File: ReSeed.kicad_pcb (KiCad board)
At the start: 2 copper layers, 60.8 x 99.9 mm, 52 parts, among them CN1 EDGE_CONNECTOR, CN2 AUDIO_OUT, CN3 AUDIO_IN, CN4 DB9_MALE, Q1 BC549C, SW1 SW_DIGIFIX, U1 MOS_8580, U105 STEPUP_MT3608, U2 CD74HCT4520E, U3 74HCT245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

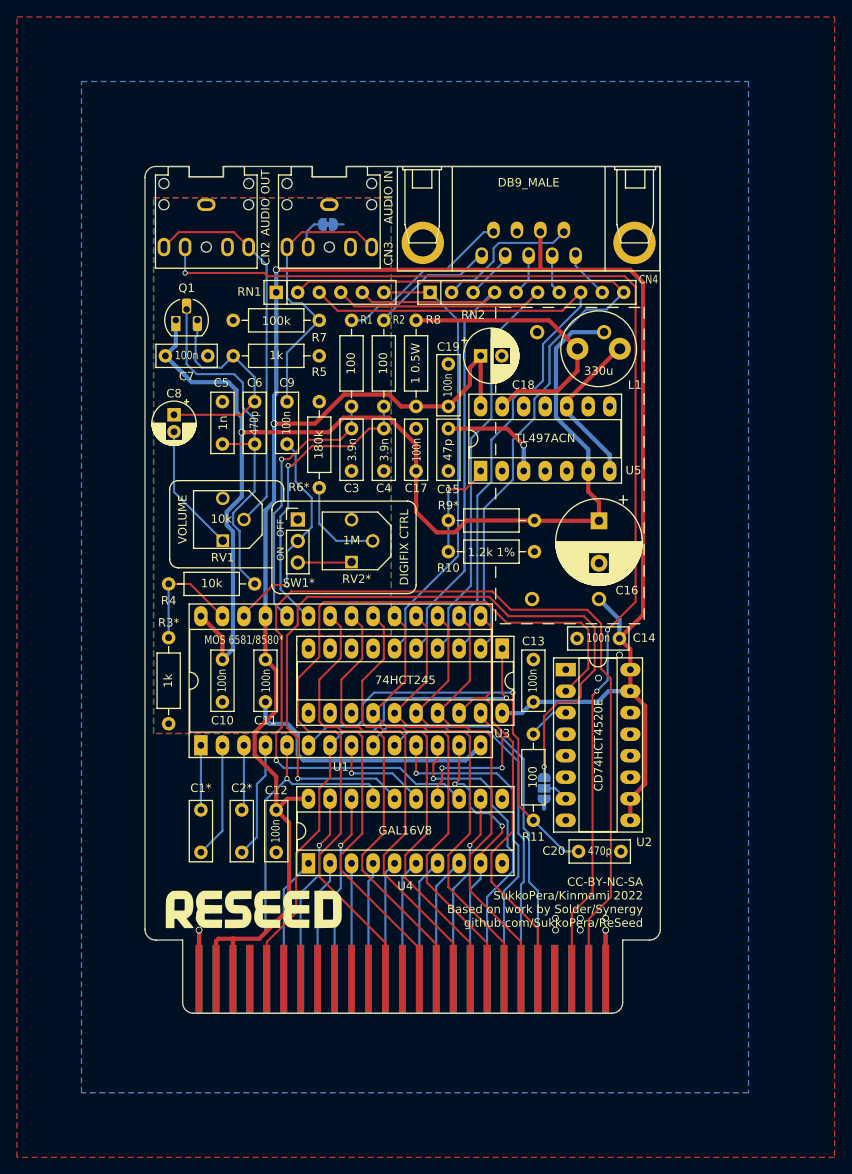
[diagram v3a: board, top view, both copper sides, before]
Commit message: Add ferrites on power lines
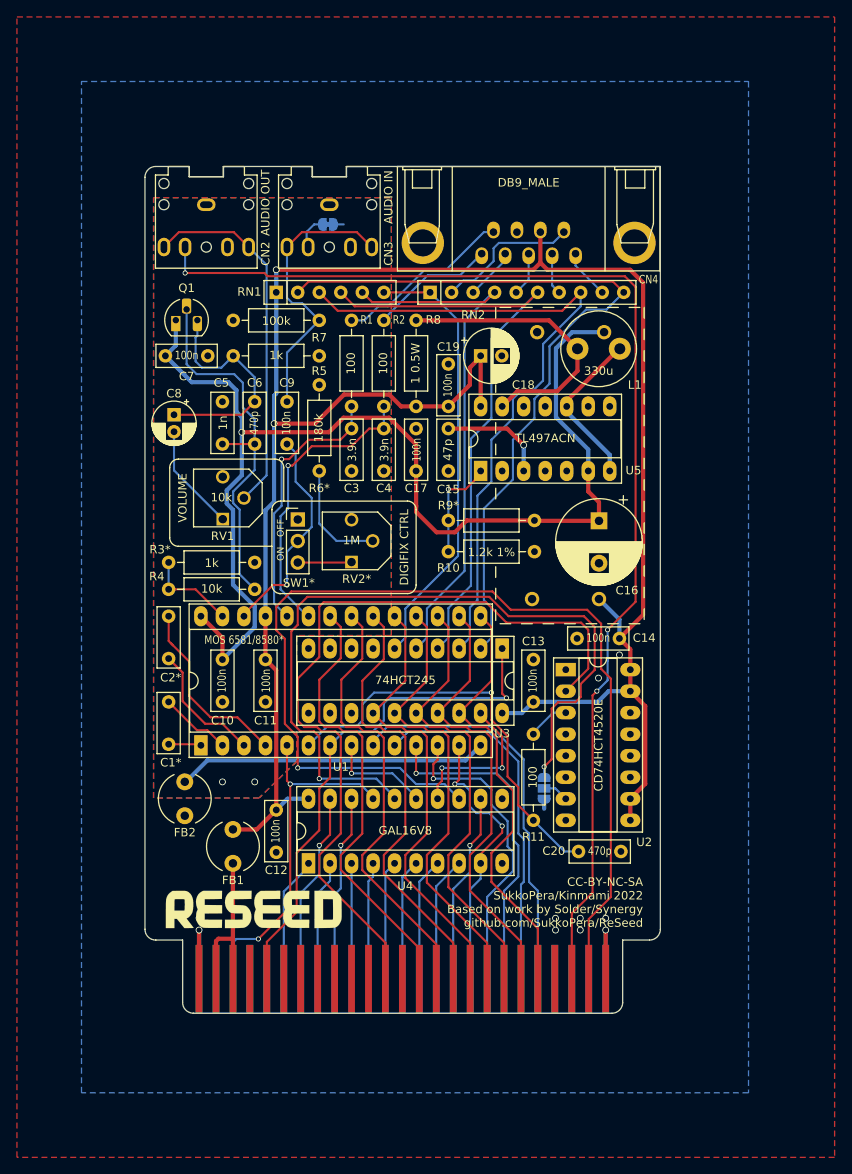
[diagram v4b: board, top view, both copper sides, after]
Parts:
- added FB1: 28C0236-0EW-10, Inductor_THT:L_Radial_D6.0mm_P4.00mm, F.Cu at (132.2, 130.4)
- added FB2: 28C0236-0EW-10, Inductor_THT:L_Radial_D6.0mm_P4.00mm, F.Cu at (126.5, 120.8)
- moved R3 21.6 mm to (134.7, 94.9), turned to 180 degrees
- moved C2 19.8 mm to (124.6, 106.2), turned to 90 degrees
- moved C1 8.64 mm to (124.6, 116.3), turned to 90 degrees
- moved RV1 2.54 mm to (132.2, 87.3)
- moved R6 1.98 mm to (142.4, 73.9)
- moved R4 0.63 mm to (134.7, 98.0)
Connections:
- CN1 pad 2: +5V -> Net-(CN1-Pad2)
- CN1 pad 3: +5V -> Net-(CN1-Pad2)
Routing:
- net +5V: track 275.3 -> 247.4 mm
- net Net-(CN1-Pad2): track 0.00 -> 20.2 mm
- net Net-(C2-Pad2): track 13.8 -> 22.2 mm
- net Net-(C2-Pad1): track 7.37 -> 15.1 mm
- net Net-(C1-Pad2): track 13.7 -> 8.47 mm
- net GNDA: track 33.5 -> 38.1 mm, vias 0 -> 2
- net Net-(C1-Pad1): track 7.37 -> 3.86 mm
- net /audio_out: track 14.3 -> 10.8 mm
- net Net-(CN2-PadR): track 45.6 -> 43.1 mm
- net Net-(C8-Pad2): track 15.2 -> 12.7 mm
- net +9V: track 138.1 -> 140.2 mm
- net Net-(R6-Pad2): track 11.4 -> 13.4 mm
- net /phi2: track 126.3 -> 124.8 mm
- net /sidclk: track 50.8 -> 49.3 mm
- net /reset: track 92.1 -> 91.1 mm
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
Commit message: Use 2-stage step-up voltage regulation @kinmami: You owe me a monument
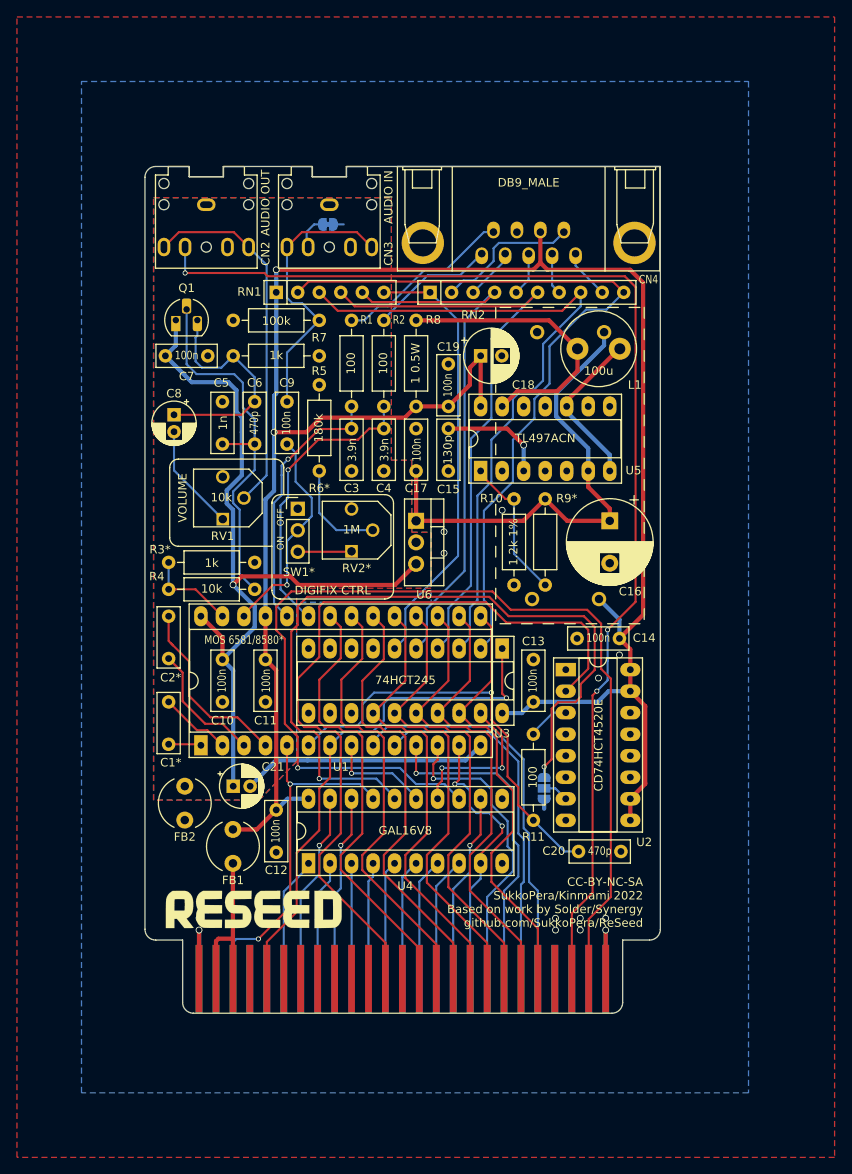
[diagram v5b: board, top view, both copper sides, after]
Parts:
- added C21: 10u, Capacitor_THT:CP_Radial_D5.0mm_P2.00mm, F.Cu at (132.2, 121.3)
- added U6: L7809, ReSeed:TO-220-3_Vertical_Round, F.Cu at (153.8, 90.0)
- C15: value 47p -> 130p
- C16: value 1000u/25V -> 3300u/25V
- L1: value 330u -> 100u
- R9: value 7.87k 1% -> 12.7k 1%
- moved R9 13.7 mm to (169.0, 97.5), turned to 90 degrees
- moved R10 4.62 mm to (165.4, 97.5), turned to 90 degrees
- moved C16 1.27 mm to (176.7, 90.0)
- moved RV2 1.27 mm to (147.4, 91.1)
- moved SW1 1.27 mm to (139.8, 88.5)
- moved FB2 0.52 mm to (126.5, 121.3)
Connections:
- C16 pad 1: +9V -> +15V
- C17 pad 1: +9V -> +15V
- R9 pad 2: +9V -> +15V
- U105 pad 1: +9V -> +15V
- U5 pad 6: +9V -> +15V
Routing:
- net +15V: track 0.00 -> 58.1 mm
- net +9V: track 140.2 -> 95.6 mm
- net GNDA: track 38.1 -> 30.7 mm, vias 2 -> 0
- net Net-(R10-Pad2): track 12.3 -> 17.2 mm, vias 1 -> 0
- net +5V: track 247.4 -> 246.6 mm
- net Net-(R6-Pad2): track 13.4 -> 12.7 mm
- net Net-(C3-Pad1): track 31.9 -> 31.3 mm
- net GND: vias 10 -> 13

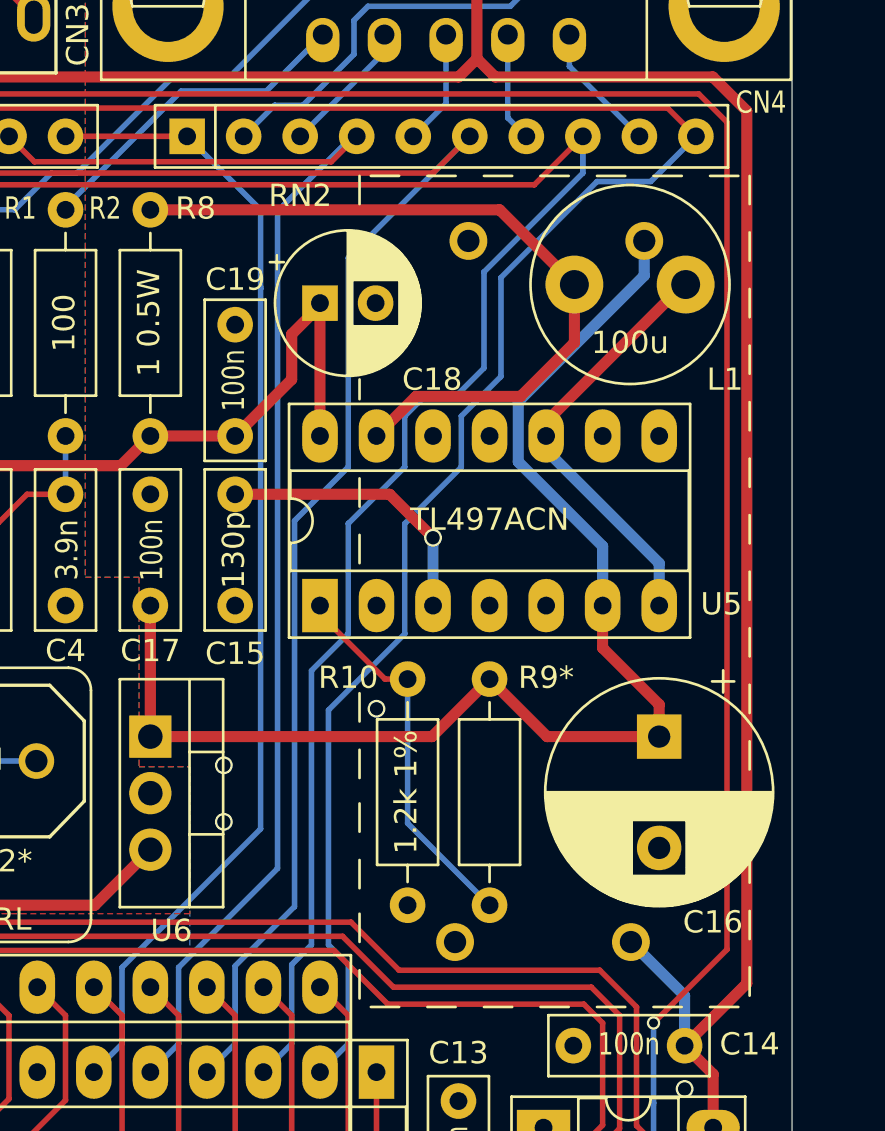
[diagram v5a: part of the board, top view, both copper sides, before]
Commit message: Silkscreen fixes
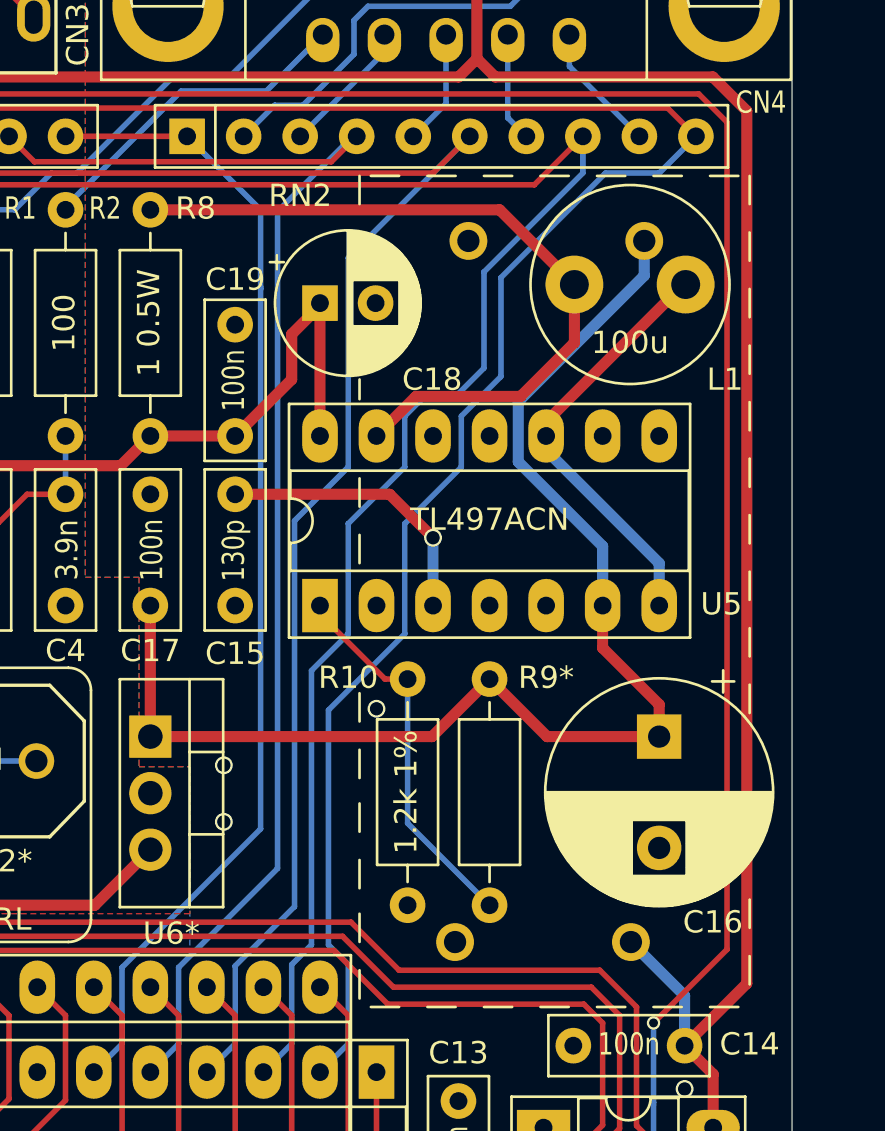
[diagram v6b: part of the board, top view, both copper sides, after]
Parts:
- moved V1 9.01 mm to (165.2, 92.3)
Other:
- board text added: "U6*"

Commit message: Add bypass jumper for 2nd regulator stage
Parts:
- added JP3: JMP_REG_BYPASS, Jumper:SolderJumper-2_P1.3mm_Open_RoundedPad1.0x1.5mm, B.Cu at (157.2, 92.5)
- moved V1 2.03 mm to (167.3, 92.3)
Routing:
- net +9V: track 95.6 -> 100.3 mm
- net +15V: track 58.1 -> 62.8 mm
- net Net-(RN1-Pad4): track 71.5 -> 73.8 mm
- net GND: vias 13 -> 12
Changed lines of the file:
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@@
     (thickness 1.6)
     (drawings 111)
-    (tracks 678)
+    (tracks 683)
     (zones 0)
-    (modules 56)
+    (modules 57)
     (nets 104)
   )
@@
   )
   (module ReSeed:cc_by_nc_sa (layer B.Cu)
-    (at 165.227 92.329 180)
+    (at 167.259 92.329 180)
     (fp_text reference V1 (at 0 0) (layer B.SilkS) hide
       (effects (font (size 1.524 1.524) (thickness 0.3)) (justify mirror))
@@
     )
   )
+  (module Jumper:SolderJumper-2_P1.3mm_Open_RoundedPad1.0x1.5mm (layer B.Cu)
+    (at 157.226 92.501323 270)
+    (descr "SMD Solder Jumper, 1x1.5mm, rounded Pads, 0.3mm gap, open")
+    (tags "solder jumper open")
+    (attr virtual)
+    (fp_text reference JP3 (at -2.204323 0 180) (layer B.SilkS)
+      (effects (font (size 1 1) (thickness 0.15)) (justify mirror))
+    )
+    (fp_text value JMP_REG_BYPASS (at 0 -1.9 90) (layer B.Fab)
+      (effects (font (size 1 1) (thickness 0.15)) (justify mirror))
+    )
+    (fp_arc (start -0.7 0.3) (end -0.7 1) (angle 90) (layer B.SilkS) (width 0.12))
+    (fp_arc (start -0.7 -0.3) (end -1.4 -0.3) (angle 90) (layer B.SilkS) (width 0.12))
+    (fp_arc (start 0.7 -0.3) (end 0.7 -1) (angle 90) (layer B.SilkS) (width 0.12))
+    (fp_arc (start 0.7 0.3) (end 1.4 0.3) (angle 90) (layer B.SilkS) (width 0.12))
+    (fp_line (start -1.4 -0.3) (end -1.4 0.3) (layer B.SilkS) (width 0.12))
+    (fp_line (start 0.7 -1) (end -0.7 -1) (layer B.SilkS) (width 0.12))
+    (fp_line (start 1.4 0.3) (end 1.4 -0.3) (layer B.SilkS) (width 0.12))
+    (fp_line (start -0.7 1) (end 0.7 1) (layer B.SilkS) (width 0.12))
+    (fp_line (start -1.65 1.25) (end 1.65 1.25) (layer B.CrtYd) (width 0.05))
+    (fp_line (start -1.65 1.25) (end -1.65 -1.25) (layer B.CrtYd) (width 0.05))
+    (fp_line (start 1.65 -1.25) (end 1.65 1.25) (layer B.CrtYd) (width 0.05))
+    (fp_line (start 1.65 -1.25) (end -1.65 -1.25) (layer B.CrtYd) (width 0.05))
+    (pad 2 smd custom (at 0.65 0 270) (size 1 0.5) (layers B.Cu B.Mask)
+      (net 8 +9V) (zone_connect 2)
+      (options (clearance outline) (anchor rect))
+      (primitives
+        (gr_circle (center 0 -0.25) (end 0.5 -0.25) (width 0))
+        (gr_circle (center 0 0.25) (end 0.5 0.25) (width 0))
+        (gr_poly (pts
+           (xy 0 0.75) (xy -0.5 0.75) (xy -0.5 -0.75) (xy 0 -0.75)) (width 0))
+      ))
+    (pad 1 smd custom (at -0.65 0 270) (size 1 0.5) (layers B.Cu B.Mask)
+      (net 103 +15V) (zone_connect 2)
+      (options (clearance outline) (anchor rect))
+      (primitives
+        (gr_circle (center 0 -0.25) (end 0.5 -0.25) (width 0))
+        (gr_circle (center 0 0.25) (end 0.5 0.25) (width 0))
+        (gr_poly (pts
+           (xy 0 0.75) (xy 0.5 0.75) (xy 0.5 -0.75) (xy 0 -0.75)) (width 0))
+      ))
+  )
   (gr_text U6* (at 154.742 98.806) (layer F.SilkS)
     (effects (font (size 1 1) (thickness 0.15)))
@@
   (via (at 170.256 136.872) (size 0.8) (drill 0.6) (layers F.Cu B.Cu) (net 4))
   (segment (start 168.91 122.839) (end 168.91 123.952) (width 0.5) (layer B.Cu) (net 4) (status 10))
-  (via (at 157.099 91.2495) (size 0.8) (drill 0.6) (layers F.Cu B.Cu) (net 4))
-  (via (at 157.099 93.7895) (size 0.8) (drill 0.6) (layers F.Cu B.Cu) (net 4))
   (via (at 163.957 88.7095) (size 0.8) (drill 0.6) (layers F.Cu B.Cu) (net 4))
+  (via (at 161.417 81.026) (size 0.8) (drill 0.6) (layers F.Cu B.Cu) (net 4))
   (segment (start 146.177 76.454) (end 146.177 79.074) (width 0.25) (layer B.Cu) (net 5) (status 30))
   (via (at 138.684 82.677) (size 0.6) (drill 0.4) (layers F.Cu B.Cu) (net 5))
@@
   (segment (start 132.207 107.604) (end 130.937 106.334) (width 0.5) (layer B.Cu) (net 8))
   (segment (start 132.207 121.285) (end 132.207 107.604) (width 0.5) (layer B.Cu) (net 8))
+  (segment (start 153.797 95.041323) (end 156.164677 95.041323) (width 0.5) (layer B.Cu) (net 8))
+  (segment (start 157.226 93.98) (end 157.226 93.151323) (width 0.5) (layer B.Cu) (net 8))
+  (segment (start 156.164677 95.041323) (end 157.226 93.98) (width 0.5) (layer B.Cu) (net 8))
   (segment (start 179.083 122.769) (end 179.083 125.309) (width 0.5) (layer F.Cu) (net 9) (status 30))
   (segment (start 179.083 107.529) (end 179.083 110.069) (width 0.5) (layer F.Cu) (net 9) (status 30))
@@
   (segment (start 176.525 110.069) (end 175.26 111.334) (width 0.5) (layer B.Cu) (net 9))
   (segment (start 179.083 110.069) (end 176.525 110.069) (width 0.5) (layer B.Cu) (net 9) (status 10))
-  (segment (start 161.417 70.485) (end 161.417 76.454) (width 0.5) (layer F.Cu) (net 9) (status 30))
+  (segment (start 161.417 70.485) (end 161.417 76.454) (width 0.5) (layer B.Cu) (net 9) (status 30))
   (via (at 137.287 60.325) (size 0.8) (drill 0.6) (layers F.Cu B.Cu) (net 9))
   (segment (start 137.287 74.93) (end 137.287 60.706) (width 0.5) (layer B.Cu) (net 9))
@@
   (segment (start 146.558 64.643) (end 166.497 64.643) (width 0.25) (layer F.Cu) (net 67))
   (segment (start 144.907 62.992) (end 146.558 64.643) (width 0.25) (layer F.Cu) (net 67) (status 10))
-  (segment (start 157.607 100.2665) (end 157.607 103.764) (width 0.25) (layer B.Cu) (net 67))
-  (segment (start 160.274 97.5995) (end 157.607 100.2665) (width 0.25) (layer B.Cu) (net 67))
-  (segment (start 157.607 103.764) (end 156.337 105.034) (width 0.25) (layer B.Cu) (net 67) (status 20))
-  (segment (start 160.274 80.264) (end 160.274 97.5995) (width 0.25) (layer B.Cu) (net 67))
-  (segment (start 162.687 77.851) (end 160.274 80.264) (width 0.25) (layer B.Cu) (net 67))
-  (segment (start 162.687 68.453) (end 162.687 77.851) (width 0.25) (layer B.Cu) (net 67))
-  (segment (start 168.148 62.992) (end 162.687 68.453) (width 0.25) (layer B.Cu) (net 67) (status 10))
+  (segment (start 162.941 64.262) (end 166.878 64.262) (width 0.25) (layer B.Cu) (net 67))
+  (segment (start 166.878 64.262) (end 168.148 62.992) (width 0.25) (layer B.Cu) (net 67))
+  (segment (start 160.274 66.929) (end 162.941 64.262) (width 0.25) (layer B.Cu) (net 67))
+  (segment (start 160.274 97.5995) (end 160.274 66.929) (width 0.25) (layer B.Cu) (net 67))
+  (segment (start 157.607 100.2665) (end 160.274 97.5995) (width 0.25) (layer B.Cu) (net 67))
+  (segment (start 157.607 103.764) (end 157.607 100.2665) (width 0.25) (layer B.Cu) (net 67))
+  (segment (start 156.337 105.034) (end 157.607 103.764) (width 0.25) (layer B.Cu) (net 67))
   (segment (start 161.925 64.135) (end 163.068 62.992) (width 0.25) (layer F.Cu) (net 68) (status 20))
   (segment (start 148.59 64.135) (end 161.925 64.135) (width 0.25) (layer F.Cu) (net 68))
@@
   (segment (start 175.987 69.25) (end 170.32699 74.91001) (width 0.5) (layer B.Cu) (net 103))
   (segment (start 175.987 67.691) (end 175.987 69.25) (width 0.5) (layer B.Cu) (net 103))
+  (segment (start 157.226 91.059) (end 157.226 91.851323) (width 0.5) (layer B.Cu) (net 103))
+  (segment (start 156.128323 89.961323) (end 157.226 91.059) (width 0.5) (layer B.Cu) (net 103))
+  (segment (start 153.797 89.961323) (end 156.128323 89.961323) (width 0.5) (layer B.Cu) (net 103))
   (zone (net 4) (net_name GND) (layer B.Cu) (hatch edge 0.508)
     (connect_pads (clearance 0.381))

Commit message: Change 3D model of ferrites
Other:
- board text added: "IN"
- board text added: "OUT"
